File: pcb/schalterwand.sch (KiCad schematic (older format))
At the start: 33 parts

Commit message: pcb: use better pin names
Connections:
- net RCLK renamed LATCH
- net SER_IN renamed MOSI
- net SRCLK renamed SCK
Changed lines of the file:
@@
 EESchema Schematic File Version 4
+LIBS:schalterwand-cache
 EELAYER 26 0
 EELAYER END
@@
 	9200 2700 9200 2800
 Text Label 8800 1800 2    50   ~ 0
-SRCLK
+SCK
 Text Label 7450 1800 2    50   ~ 0
-SRCLK
+SCK
 Text Label 6000 1800 2    50   ~ 0
-SRCLK
+SCK
 Text Label 3750 1400 2    50   ~ 0
-SRCLK
+SCK
 Text Label 7450 2100 2    50   ~ 0
-RCLK
+LATCH
 Text Label 8800 2100 2    50   ~ 0
-RCLK
+LATCH
 Text Label 6000 2100 2    50   ~ 0
-RCLK
-Text Label 3750 1600 2    50   ~ 0
-RCLK
+LATCH
 $Comp
 L power:VCC #PWR?
@@
 	4200 4950 4200 5100
 Text Label 3700 3850 2    50   ~ 0
-SRCLK
-Text Label 4700 4050 0    50   ~ 0
-RCLK
+SCK
 Text Label 3700 3750 2    50   ~ 0
 Bl2
@@
 Bl3
 Text Label 6000 1600 2    50   ~ 0
-SER_IN
+MOSI
 Text Label 4250 1600 0    50   ~ 0
-SER_IN
+MOSI
 Text Label 3700 4550 2    50   ~ 0
-SER_IN
+MOSI
+Text Label 3750 1600 2    50   ~ 0
+LATCH
+Text Label 4700 4050 0    50   ~ 0
+LATCH
 $EndSCHEMATC

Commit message: pcb: add pulldown resistors to MOSI, SCK and LATCH
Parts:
- added R? (x3): 4k7, symbol Device:R
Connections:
- net GND: now also R?.2, R?.2, R?.2
- net LATCH: now also R?.1
- net MOSI: now also R?.1
- net SCK: now also R?.1
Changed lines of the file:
@@
 L power:GND #PWR?
 U 1 1 5C0C3B6E
-P 3350 1800
-F 0 "#PWR?" H 3350 1550 50  0001 C CNN
-F 1 "GND" H 3355 1627 50  0000 C CNN
-F 2 "" H 3350 1800 50  0001 C CNN
-F 3 "" H 3350 1800 50  0001 C CNN
-	1    3350 1800
-	1    0    0    -1
-$EndComp
-Wire Wire Line
-	3750 1500 3350 1500
-Wire Wire Line
-	3350 1500 3350 1800
+P 3250 2000
+F 0 "#PWR?" H 3250 1750 50  0001 C CNN
+F 1 "GND" H 3255 1827 50  0000 C CNN
+F 2 "" H 3250 2000 50  0001 C CNN
+F 3 "" H 3250 2000 50  0001 C CNN
+	1    3250 2000
+	1    0    0    -1
+$EndComp
 $Comp
 L power:GND #PWR?
 U 1 1 5C0C3C16
-P 4800 1800
-F 0 "#PWR?" H 4800 1550 50  0001 C CNN
-F 1 "GND" H 4805 1627 50  0000 C CNN
-F 2 "" H 4800 1800 50  0001 C CNN
-F 3 "" H 4800 1800 50  0001 C CNN
-	1    4800 1800
-	1    0    0    -1
-$EndComp
-Wire Wire Line
-	4800 1800 4800 1500
+P 4800 2000
+F 0 "#PWR?" H 4800 1750 50  0001 C CNN
+F 1 "GND" H 4805 1827 50  0000 C CNN
+F 2 "" H 4800 2000 50  0001 C CNN
+F 3 "" H 4800 2000 50  0001 C CNN
+	1    4800 2000
+	1    0    0    -1
+$EndComp
 Wire Wire Line
 	4250 1500 4800 1500
@@
 Text Label 6000 1800 2    50   ~ 0
 SCK
-Text Label 3750 1400 2    50   ~ 0
+Text Label 2900 1400 2    50   ~ 0
 SCK
 Text Label 7450 2100 2    50   ~ 0
@@
 Text Label 6000 1600 2    50   ~ 0
 MOSI
-Text Label 4250 1600 0    50   ~ 0
+Text Label 4600 1600 0    50   ~ 0
 MOSI
 Text Label 3700 4550 2    50   ~ 0
 MOSI
-Text Label 3750 1600 2    50   ~ 0
+Text Label 3500 1600 2    50   ~ 0
 LATCH
 Text Label 4700 4050 0    50   ~ 0
 LATCH
+Wire Wire Line
+	3250 1500 3750 1500
+$Comp
+L Device:R R?
+U 1 1 5C10181E
+P 3550 1750
+F 0 "R?" H 3400 1750 50  0000 L CNN
+F 1 "4k7" V 3550 1700 50  0000 L CNN
+F 2 "" V 3480 1750 50  0001 C CNN
+F 3 "~" H 3550 1750 50  0001 C CNN
+	1    3550 1750
+	1    0    0    -1
+$EndComp
+Wire Wire Line
+	3500 1600 3550 1600
+Wire Wire Line
+	3750 1600 3550 1600
+Connection ~ 3550 1600
+$Comp
+L power:GND #PWR?
+U 1 1 5C10B203
+P 3550 2000
+F 0 "#PWR?" H 3550 1750 50  0001 C CNN
+F 1 "GND" H 3555 1827 50  0000 C CNN
+F 2 "" H 3550 2000 50  0001 C CNN
+F 3 "" H 3550 2000 50  0001 C CNN
+	1    3550 2000
+	1    0    0    -1
+$EndComp
+Wire Wire Line
+	3550 1900 3550 2000
+Wire Wire Line
+	3250 1500 3250 2000
+Wire Wire Line
+	4800 1500 4800 2000
+$Comp
+L Device:R R?
+U 1 1 5C1150D5
+P 3000 1750
+F 0 "R?" H 2850 1750 50  0000 L CNN
+F 1 "4k7" V 3000 1700 50  0000 L CNN
+F 2 "" V 2930 1750 50  0001 C CNN
+F 3 "~" H 3000 1750 50  0001 C CNN
+	1    3000 1750
+	1    0    0    -1
+$EndComp
+Wire Wire Line
+	3750 1400 3000 1400
+Wire Wire Line
+	3000 1600 3000 1400
+Wire Wire Line
+	3000 1400 2900 1400
+Connection ~ 3000 1400
+$Comp
+L power:GND #PWR?
+U 1 1 5C1225F1
+P 3000 2000
+F 0 "#PWR?" H 3000 1750 50  0001 C CNN
+F 1 "GND" H 3005 1827 50  0000 C CNN
+F 2 "" H 3000 2000 50  0001 C CNN
+F 3 "" H 3000 2000 50  0001 C CNN
+	1    3000 2000
+	1    0    0    -1
+$EndComp
+Wire Wire Line
+	3000 1900 3000 2000
+$Comp
+L power:GND #PWR?
+U 1 1 5C1298F3
+P 4550 2000
+F 0 "#PWR?" H 4550 1750 50  0001 C CNN
+F 1 "GND" H 4555 1827 50  0000 C CNN
+F 2 "" H 4550 2000 50  0001 C CNN
+F 3 "" H 4550 2000 50  0001 C CNN
+	1    4550 2000
+	1    0    0    -1
+$EndComp
+Wire Wire Line
+	4250 1600 4550 1600
+$Comp
+L Device:R R?
+U 1 1 5C13496E
+P 4550 1750
+F 0 "R?" H 4400 1750 50  0000 L CNN
+F 1 "4k7" V 4550 1700 50  0000 L CNN
+F 2 "" V 4480 1750 50  0001 C CNN
+F 3 "~" H 4550 1750 50  0001 C CNN
+	1    4550 1750
+	1    0    0    -1
+$EndComp
+Connection ~ 4550 1600
+Wire Wire Line
+	4550 1600 4600 1600
+Wire Wire Line
+	4550 1900 4550 2000
 $EndSCHEMATC

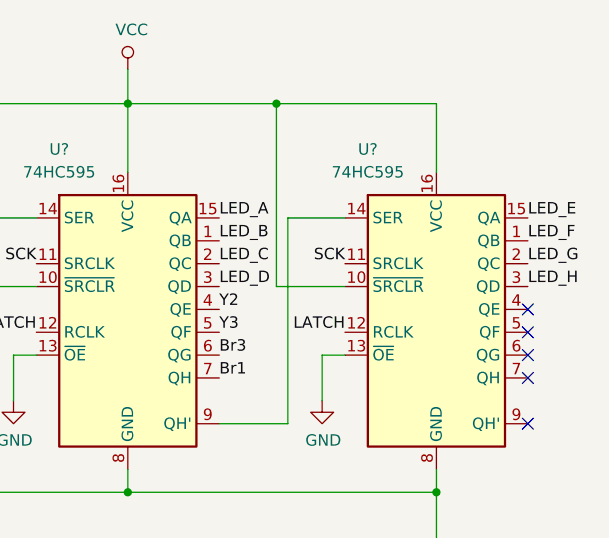
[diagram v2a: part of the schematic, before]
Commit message: pcb: correct LED mappings
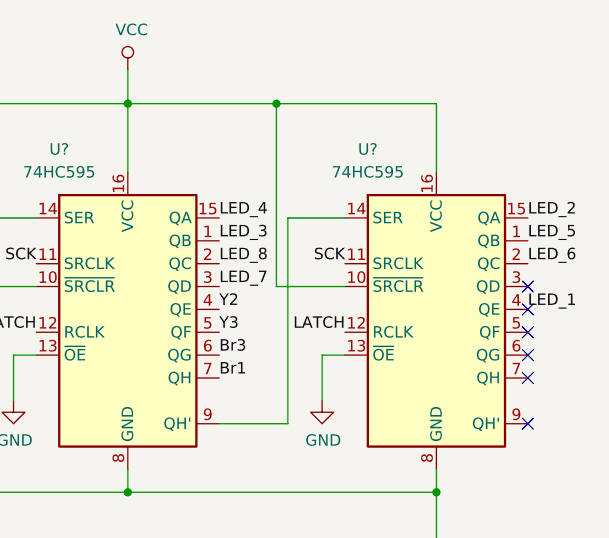
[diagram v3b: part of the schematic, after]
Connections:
- net LED_1: now reaches U?.4 (QE)
- net LED_A renamed LED_4
- net LED_B renamed LED_3
- net LED_C renamed LED_8
- net LED_D renamed LED_7
- net LED_E renamed LED_2
- net LED_F renamed LED_5
- net LED_G renamed LED_6
- net LED_H: no longer names the net of U?.3 (QD)
- no-connect marks 11 -> 12
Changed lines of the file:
@@
 LED8
 Text Label 8250 1600 0    50   ~ 0
-LED_A
+LED_4
 Wire Wire Line
 	8550 1600 8550 2500
@@
 	7850 1100 8500 1100
 Text Label 8250 1700 0    50   ~ 0
-LED_B
+LED_3
 Text Label 8250 1800 0    50   ~ 0
-LED_C
+LED_8
 Text Label 8250 1900 0    50   ~ 0
-LED_D
+LED_7
 NoConn ~ 9600 2000
 NoConn ~ 9600 2100
@@
 NoConn ~ 9600 2300
 Text Label 9600 1600 0    50   ~ 0
-LED_E
+LED_2
 Text Label 9600 1800 0    50   ~ 0
-LED_G
+LED_6
 Text Label 9600 1700 0    50   ~ 0
-LED_F
-Text Label 9600 1900 0    50   ~ 0
-LED_H
+LED_5
+Text Label 9600 2000 0    50   ~ 0
+LED_1
 $Comp
 L MCU_Module:Arduino_UNO_R2 A?
@@
 Wire Wire Line
 	4550 1900 4550 2000
+NoConn ~ 9600 1900
 $EndSCHEMATC

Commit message: pcb: add raspberry pi
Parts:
- added J?: Raspberry_Pi_2_3, symbol Connector:Raspberry_Pi_2_3
- gave numbers to parts that had none: 36
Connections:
- net GND: now also J?.14 (GND), J?.20 (GND), J?.25 (GND), J?.30 (GND), J?.34 (GND), J?.39 (GND), J?.6 (GND), J?.9 (GND)
- net VCC: now also J?.2 (5V), J?.4 (5V)
- net at A1.15 (D0/RX): now also J?.8 (GPIO14/TXD)
- net at A1.16 (D1/TX): now also J?.10 (GPIO15/RXD)
- no-connect marks 12 -> 55
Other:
- moved on the sheet: A1, D13, D14, D15, D16, D17, D18, D19, D20, R10, R11, R4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
